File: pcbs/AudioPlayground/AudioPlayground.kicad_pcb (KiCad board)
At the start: 6 copper layers, 69.7 x 22.9 mm, 149 parts, among them J1 Conn_01x07_Socket, J2 Conn_Battery, J3 USB_C_Receptacle_USB2.0_14P, J4 TC2030, J5 Conn_01x12_Pin, J7 Conn_01x16_Pin, J9 Conn_01x07_Socket, U1 nRF5340-QKxx, U10 MCP73831-2-OT, U11 74LVC1GU04DRL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

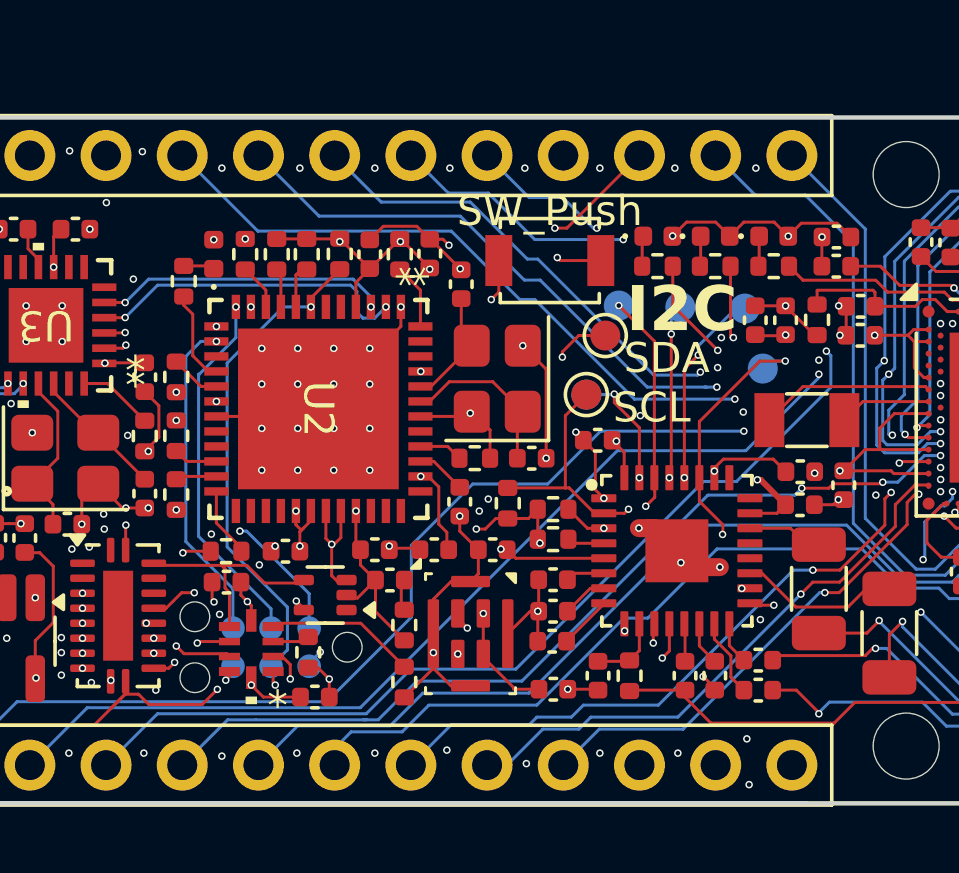
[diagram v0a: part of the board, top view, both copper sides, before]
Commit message: Fix Silkscreen
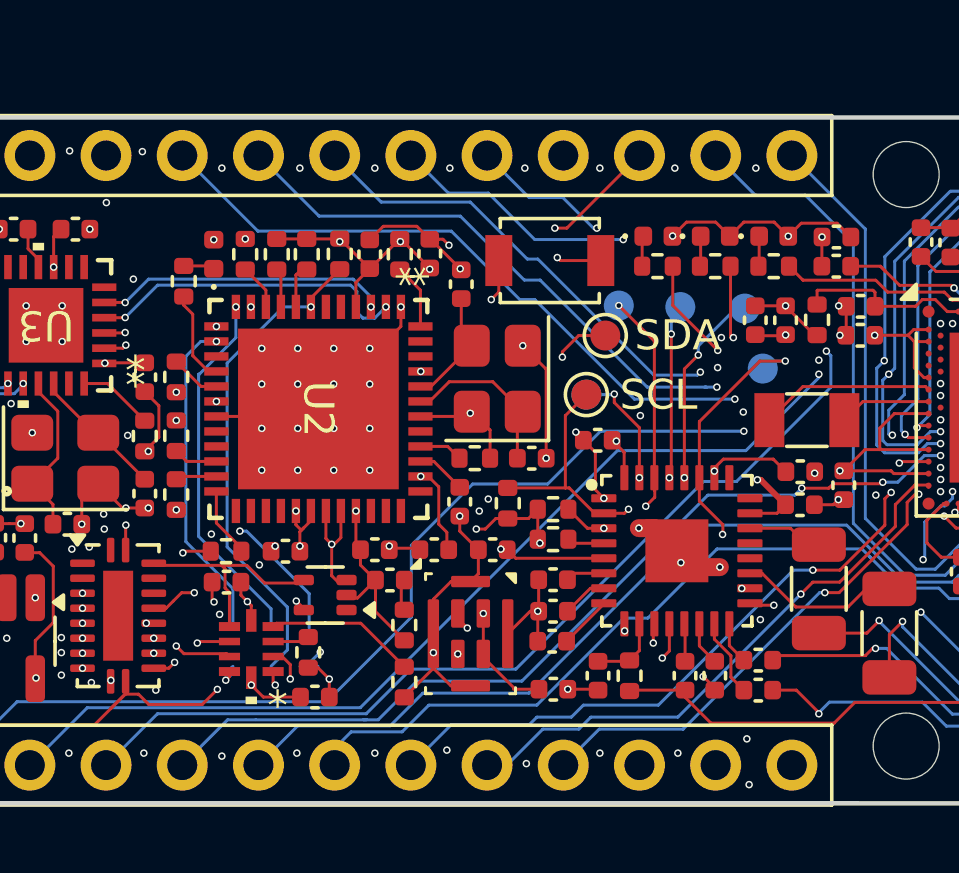
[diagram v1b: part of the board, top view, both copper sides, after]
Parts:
- removed J4: TC2030, Connector:Tag-Connect_TC2030-IDC-NL_2x03_P1.27mm_Vertical
- moved G*** 12.1 mm to (145.1, 135.7)
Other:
- board text added: "LE Audio Playground v2.0"
- board text added: "PCB Design: Fabian Schmid"
- board text removed: "Fabian Schmid"
- board text removed: "I2C"
- board text removed: "I2S"
- board text removed: "LEAudio DevBoard v1.1"

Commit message: Update MICs
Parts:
- removed C68, C69: 100nF, Capacitor_SMD:C_0402_1005Metric
- removed R32: 150R, Resistor_SMD:R_0402_1005Metric
- removed R35: 10k, Resistor_SMD:R_0402_1005Metric
- removed R36, R37: 27R, Resistor_SMD:R_0402_1005Metric
- added G***: LOGO, LOGO, B.Cu at (116.7, 131.0)
- added U16: SN74LVC1G126DRYR(UMW), SN74LVC1G126DRYR:SN74LVC1G126DRYR, F.Cu at (117.6, 140.3)
- added U17: SN74LVC1G126DRYR(UMW), SN74LVC1G126DRYR:SN74LVC1G126DRYR, F.Cu at (118.6, 136.4)
- added U18: SN74LVC1G126DRYR(UMW), SN74LVC1G126DRYR:SN74LVC1G126DRYR, F.Cu at (118.6, 138.3)
- added U19: GTD3526BA-1N, GTD3526BA-1N:GTD3526BA-1N, F.Cu at (124.7, 138.7)
- added U20: GTD3526BA-1N, GTD3526BA-1N:GTD3526BA-1N, F.Cu at (152.0, 139.0)
- U11: value 74LVC1GU04DRL -> SN74LVC1G126DRYR(UMW); footprint Package_TO_SOT_SMD:SOT-553 -> SN74LVC1G126DRYR:SN74LVC1G126DRYR
- U13: value 74CBTLV3245 -> SN74LVC1G126DRYR(UMW); footprint Package_DFN_QFN:DHVQFN-20-1EP_2.5x4.5mm_P0.5mm_EP1x3mm -> SN74LVC1G126DRYR:SN74LVC1G126DRYR
- moved U11 7.39 mm to (116.5, 136.4), turned to -90 degrees
- moved U7 4.38 mm to (147.8, 139.3), turned to 90 degrees
- moved C70 2.56 mm to (121.0, 140.5)
- moved C44 2.43 mm to (149.9, 136.6)
- moved U14 1.07 mm to (121.0, 138.2)
- moved U13 0.50 mm to (116.5, 138.3), turned to -90 degrees
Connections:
- net Net-(U12-EN) renamed /Power/ST
- U1 pad AK4: /MCU/SWD.SWO -> unconnected-(U1-CSN/TRACEDATA0/P0.11-PadAK4)
- U11 pad 1: unconnected-(U11-NC-Pad1) -> +3.3V_SWITCHED
- U11 pad 2: +3.3V_SWITCHED -> /Interface MCU/VCOM.TXD
- U11 pad 4: Net-(U13-OE) -> /MCU/VCOM.RXD
- U11 pad 5: +3.3V -> unconnected-(U11-NC-Pad5)
- U13 pad 1: unconnected-(U13-NC-Pad1) -> +3.3V_SWITCHED
- U13 pad 2: unconnected-(U13-A1-Pad2) -> /Interface MCU/VCOM.RXD
- U13 pad 3: unconnected-(U13-A2-Pad3) -> GND
- U13 pad 4: /Interface MCU/VCOM.TXD -> /MCU/VCOM.TXD
- U13 pad 5: /Interface MCU/VCOM.RXD -> unconnected-(U13-NC-Pad5)
- U13 pad 6: /Interface MCU/SWD.SWDIO -> +3.3V
- U14 pad 1: /MCU/D+ -> unconnected-(U14-1D+-Pad1)
- U14 pad 2: /MCU/D- -> unconnected-(U14-1D--Pad2)
- U14 pad 3: Net-(U14-2D+) -> /MCU/D+
- U14 pad 4: Net-(U14-2D-) -> /MCU/D-
- U14 pad 6: Net-(U13-OE) -> GND
- U14 pad 9: GND -> +3.3V_SWITCHED
- U2 pad 36: /Interface MCU/P100 -> unconnected-(U2-P100-Pad36)
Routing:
- net /MCU/SWD.SWO: track 29.8 -> 0.00 mm, vias 3 -> 0
- net GND: track 102.2 -> 82.6 mm, vias 267 -> 245
- net Net-(U2-RES): track 16.4 -> 1.65 mm, vias 1 -> 0
- net Net-(U2-P300/TCK/SWCLK): track 12.2 -> 0.00 mm, vias 1 -> 0
- net /Audio Codec/DIGMICDATA: track 25.3 -> 37.0 mm, vias 4 -> 3
- net unconnected-(U1-CSN/TRACEDATA0/P0.11-PadAK4): track 0.00 -> 11.0 mm, vias 0 -> 2
- net /Audio Codec/DIGMICCLK: track 26.3 -> 34.8 mm, vias 4 -> 5
- net +3.3V_SWITCHED: track 92.1 -> 100.1 mm, vias 17 -> 22
- net Net-(U13-OE): track 7.17 -> 0.00 mm
- net /Interface MCU/SWD.SWO: track 5.68 -> 0.00 mm, vias 2 -> 0
- net Net-(U14-2D-): track 5.02 -> 0.00 mm
- net Net-(U2-P108/TMS/SWDIO): track 11.5 -> 7.37 mm
- net +3.3V: track 84.2 -> 80.1 mm, vias 29 -> 35
- net /Interface MCU/SWD.SWDCLK: track 8.82 -> 5.17 mm
- net /MCU/VCOM.TXD: track 34.6 -> 38.2 mm
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
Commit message: Fix unconnected traces
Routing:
- net Net-(U2-P109/TDO/SWO): track 7.40 -> 0.00 mm
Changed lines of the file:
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@@
-	(segment
-		(start 121.018949 135.268949)
-		(end 121.243949 135.268949)
-		(width 0.1)
-		(layer "B.Cu")
-		(net 37)
-	)
 	(segment
 		(start 121.018949 135.268949)
@@
 		(net 38)
 	)
-	(segment
-		(start 119.218949 129.443949)
-		(end 119.218949 135.618949)
-		(width 0.1)
-		(layer "B.Cu")
-		(net 38)
-	)
-	(segment
-		(start 119.716801 128.946097)
-		(end 119.218949 129.443949)
-		(width 0.1)
-		(layer "B.Cu")
-		(net 38)
-	)
-	(segment
-		(start 120.235845 128.946097)
-		(end 119.716801 128.946097)
-		(width 0.1)
-		(layer "B.Cu")
-		(net 38)
-	)

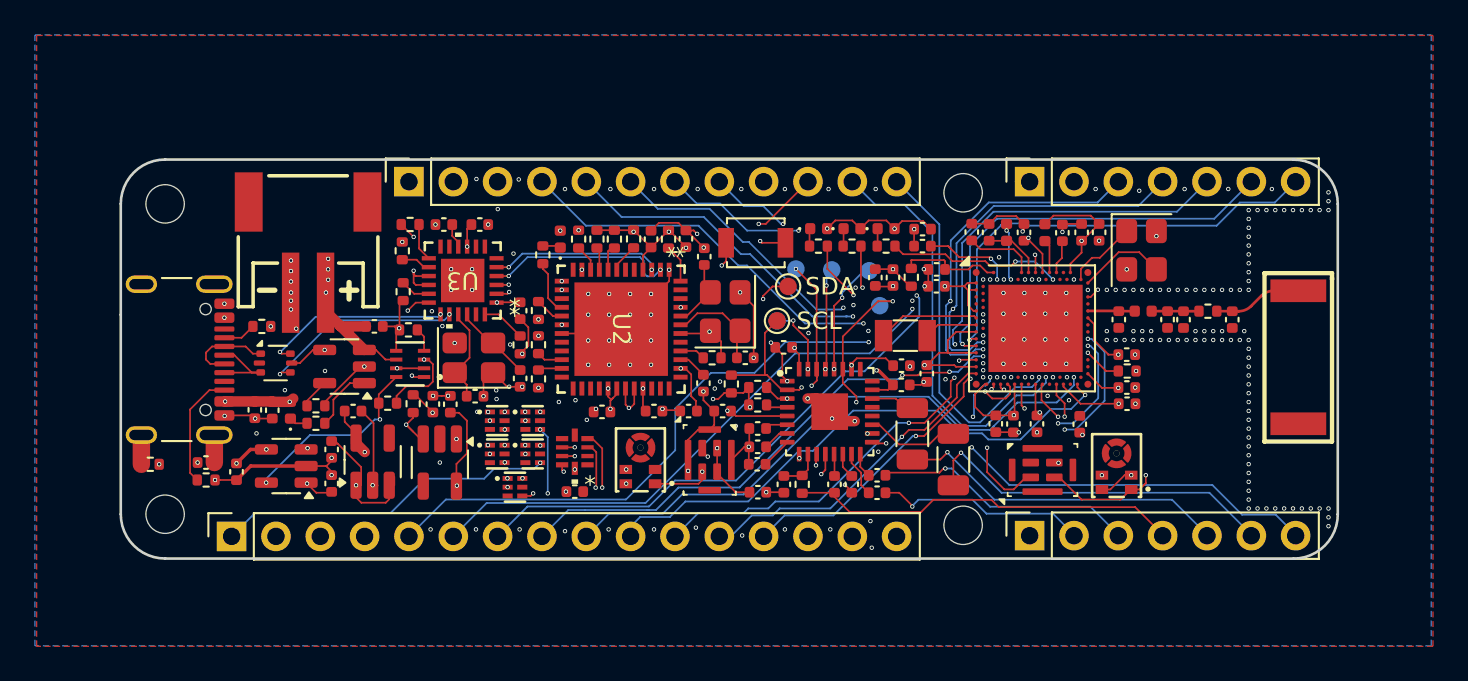
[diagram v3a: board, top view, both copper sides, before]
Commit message: Fix Codec IRQ
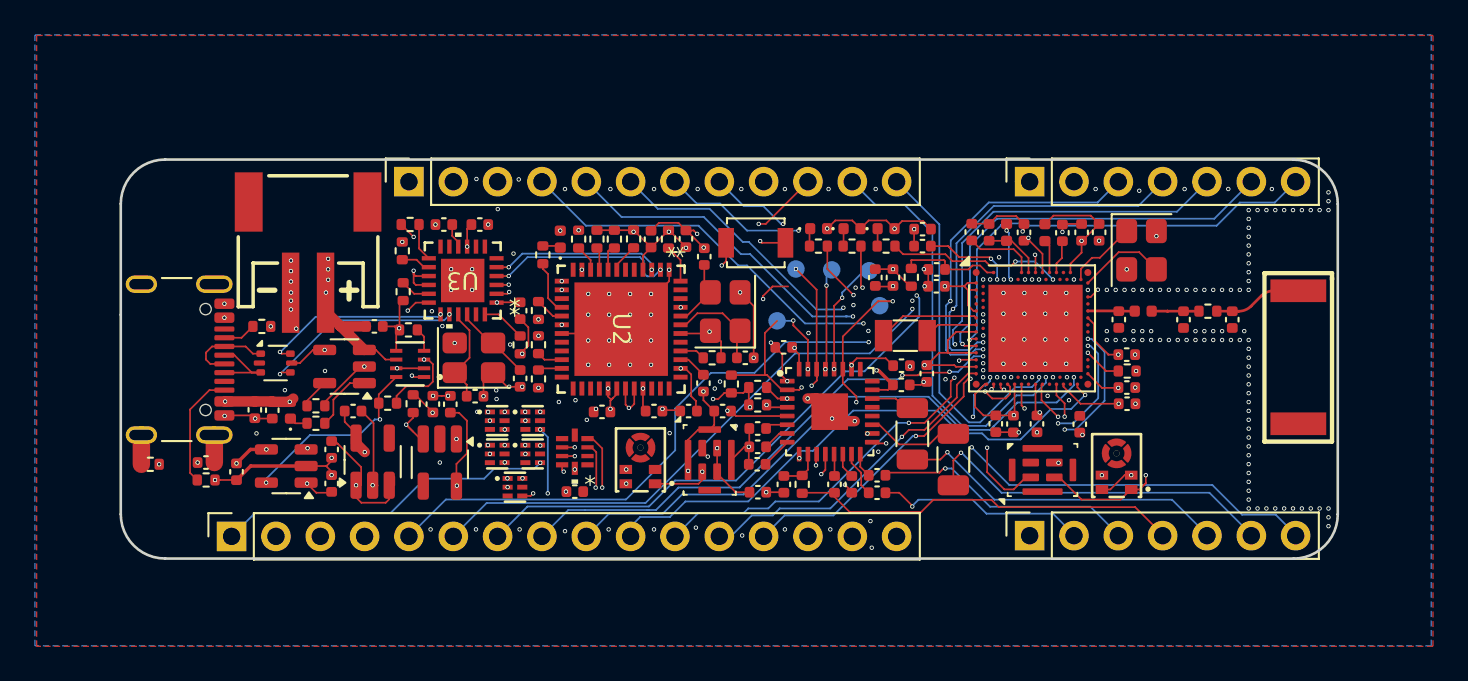
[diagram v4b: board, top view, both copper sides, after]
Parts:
- removed C20: NC, Capacitor_SMD:C_0402_1005Metric
- removed REF** (x4): MountingHole_2.2mm_M2, MountingHole:MountingHole_2.2mm_M2
- removed TP1: SDA, TestPoint:TestPoint_Pad_D1.0mm
- removed TP2: SCL, TestPoint:TestPoint_Pad_D1.0mm
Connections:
- R11 pad 2: Net-(U4-IRQ) -> /Audio Codec/IRQ
- U1 pad AK4: unconnected-(U1-CSN/TRACEDATA0/P0.11-PadAK4) -> /Audio Codec/IRQ
- U4 pad 4: Net-(U4-IRQ) -> /Audio Codec/IRQ
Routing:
- net /Audio Codec/IRQ: track 0.00 -> 27.9 mm, vias 0 -> 4
- net unconnected-(U1-CSN/TRACEDATA0/P0.11-PadAK4): track 11.0 -> 0.00 mm, vias 2 -> 0
- net Net-(U4-IRQ): track 1.24 -> 0.00 mm
